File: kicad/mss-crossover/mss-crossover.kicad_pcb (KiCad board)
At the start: 2 copper layers, 76.2 x 57.2 mm, 64 parts, among them J1 Screw_Terminal_01x02, J10 SM04B-SRSS, J2 Screw_Terminal_01x02, J3 Screw_Terminal_01x02, J4 Screw_Terminal_01x02, J5 690-005-299-043, J6 SM04B-SRSS, J7 Micro_SD_Card_Det_Hirose_DM3AT, J8 Screw_Terminal_01x02, J9 Conn_01x05, SW1 FSM4JSMATR, SW2 FSM4JSMATR, U1 AP63203WU, U2 ESP32-S2-SOLO, U3 MAX98357AETE+T

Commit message: Initial PCB layout complete on v2.0
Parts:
- removed C10, C11, C12, C14, C15, C16, C17: 1uF, Capacitor_SMD:C_0805_2012Metric
- removed C13, C7, C9: 0.1uF, Capacitor_SMD:C_0805_2012Metric
- removed C8: 10uF, Capacitor_SMD:C_0805_2012Metric
- removed J10, J6: SM04B-SRSS, Connector_JST:JST_SH_SM04B-SRSS-TB_1x04-1MP_P1.00mm_Horizontal
- removed J5: 690-005-299-043, digikey-footprints:USB_Mini_B_Female_690-005-299-043
- removed J7: Micro_SD_Card_Det_Hirose_DM3AT, Connector_Card:microSD_HC_Hirose_DM3AT-SF-PEJM5
- removed J8: Screw_Terminal_01x02, TerminalBlock_MetzConnect:TerminalBlock_MetzConnect_Type059_RT06303HBWC_1x03_P3.50mm_Horizontal
- removed J9: Conn_01x05, Connector_PinHeader_2.54mm:PinHeader_1x05_P2.54mm_Vertical
- removed JP1, JP2: Conn_01x02, Connector_PinHeader_2.54mm:PinHeader_1x02_P2.54mm_Vertical
- removed L1: 4.7uH, ISE_UltraLibrarian:MSS6132-xxxMLC
- removed R10, R11, R12, R9: 1k, Resistor_SMD:R_0805_2012Metric
- removed R13, R14, R8: 10k, Resistor_SMD:R_0805_2012Metric
- removed R7: DNI, Resistor_SMD:R_0805_2012Metric
- removed SW2: FSM4JSMATR, digikey-footprints:Switch_Tactile_SMD_6x6mm
- removed TP1, TP2, TP3, TP4, TP5, TP6: TestPoint, TestPoint:TestPoint_Pad_D2.0mm
- added D6: GREEN LED, LED_SMD:LED_0805_2012Metric, F.Cu at (51.8, 187.6)
- added D7: RED LED, LED_SMD:LED_0805_2012Metric, F.Cu at (66.5, 187.6)
- added D8: AMBER LED, LED_SMD:LED_0805_2012Metric, F.Cu at (58.8, 187.6)
- added D9: SMAJ18A-TP, Diode_SMD:D_SMA, F.Cu at (71.4, 175.1)
- added F1: 1210L020WR, Resistor_SMD:R_1210_3225Metric, F.Cu at (69.7, 165.7)
- added T1: PE-51687, ISE_Generic:XFMR_PE-51687, F.Cu at (44.3, 159.2)
- added U4: TLP241A, ISE_UltraLibrarian:11-5B201S_TOS, F.Cu at (66.0, 175.1)
- C2: value 10uF -> 22uF
- C3: value 0.1uF -> 1uF
- C4, C5: value 22uF -> 0.1uF
- C6: value 10uF -> 0.1uF
- D1, D2: value D_Schottky -> CDBM140G
- D3: value GREEN LED -> CDBM140G; footprint LED_SMD:LED_0805_2012Metric -> Diode_SMD:D_SOD-123
- D4: value RED LED -> CDBM140G; footprint LED_SMD:LED_0805_2012Metric -> Diode_SMD:D_SOD-123
- D5: value RED LED -> BAV99; footprint LED_SMD:LED_0805_2012Metric -> Package_TO_SOT_SMD:SOT-23
- J2: value Screw_Terminal_01x02 -> AVR-ISP; footprint TerminalBlock_MetzConnect:TerminalBlock_MetzConnect_Type059_RT06303HBWC_1x03_P3.50mm_Horizontal -> Connector:Tag-Connect_TC2030-IDC-NL_2x03_P1.27mm_Vertical
- J3, J4: value Screw_Terminal_01x02 -> 8P8C; footprint TerminalBlock_MetzConnect:TerminalBlock_MetzConnect_Type059_RT06303HBWC_1x03_P3.50mm_Horizontal -> Connector_RJ:RJ45_Amphenol_54602-x08_Horizontal
- R3: value 330 -> 1k
- R4: value 330 -> 510
- R5: value 330 -> 100k
- R6: value DNI -> 330
- SW1: footprint digikey-footprints:Switch_Tactile_SMD_6x6mm -> ISE_Generic:TE_FSM4JSMA
- U1: value AP63203WU -> AP7381-33Y; footprint Package_TO_SOT_SMD:TSOT-23-6 -> ISE_Generic:SOT-89-3
- U2: value ESP32-S2-SOLO -> INA180A4; footprint Espressif:ESP32-S2-SOLO -> Package_TO_SOT_SMD:SOT-23-5
- U3: value MAX98357AETE+T -> ATtiny85-20S; footprint ISE_UltraLibrarian:21-0136I_T1633-4_MXM -> Package_SO:SOIC-8W_5.3x5.3mm_P1.27mm
- moved D4 59.2 mm to (30.6, 168.9), turned to -90 degrees
- moved D5 50.2 mm to (44.9, 167.1), turned to -90 degrees
- moved R6 47.0 mm to (64.9, 182.5)
- moved U3 36.8 mm to (55.5, 180.1)
- moved R4 36.0 mm to (48.5, 167.1)
- moved SW1 34.2 mm to (61.0, 161.0), turned to -90 degrees
- moved R5 27.5 mm to (59.0, 172.2), turned to 180 degrees
- moved C6 24.4 mm to (51.4, 167.1), turned to -90 degrees
- moved R1 23.8 mm to (51.8, 185.0), turned to 180 degrees
- moved U2 21.8 mm to (54.7, 171.1), turned to 180 degrees
- moved U1 19.9 mm to (42.8, 186.3), turned to -90 degrees
- moved D3 19.8 mm to (39.8, 168.9), turned to -90 degrees
- moved J4 19.6 mm to (86.7, 167.8), turned to 180 degrees
- moved H3 19.2 mm to (94.7, 158.0)
- moved H4 19.1 mm to (29.7, 158.0)
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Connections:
- C2 pad 1: /VPWR -> +3.3V
- C3 pad 1: Net-(C3-Pad1) -> /DCC_CURRENT
- C3 pad 2: Net-(C3-Pad2) -> GND
- C4 pad 1: +3.3V -> //CAL_SW
- C6 pad 1: +3.3V -> Net-(D5-Pad1)
- C6 pad 2: GND -> +3.3V
- D3 pad 1: GND -> Net-(D2-Pad2)
- D3 pad 2: Net-(D3-Pad2) -> GND
- D4 pad 1: GND -> Net-(D1-Pad2)
- D4 pad 2: Net-(D4-Pad2) -> GND
- D5 pad 1: GND -> Net-(D5-Pad1)
- D5 pad 2: Net-(D5-Pad2) -> Net-(D5-Pad1)
- J1 pad 1: Net-(D2-Pad2) -> Net-(D1-Pad2)
- J1 pad 2: GND -> Net-(D2-Pad2)
- J2 pad 1: /VPWR -> Net-(J2-Pad1)
- J2 pad 2: /VPWR -> +3.3V
- J2 pad 3: /VPWR -> Net-(J2-Pad3)
- J3 pad 1: GND -> Net-(J3-Pad1)
- J3 pad 2: GND -> Net-(J3-Pad2)
- J3 pad 3: GND -> Net-(J3-Pad3)
- J4 pad 1: Net-(J4-Pad1) -> Net-(J3-Pad3)
- J4 pad 2: GND -> Net-(J3-Pad6)
- J4 pad 3: Net-(J4-Pad3) -> Net-(J3-Pad1)
- R1 pad 1: Net-(J4-Pad1) -> Net-(D6-Pad2)
- R1 pad 2: /EN1 -> +3.3V
- R2 pad 1: Net-(J4-Pad3) -> Net-(J2-Pad1)
- R2 pad 2: /EN2 -> Net-(R2-Pad2)
- R3 pad 1: Net-(D3-Pad2) -> Net-(J2-Pad4)
- R3 pad 2: +3.3V -> Net-(R3-Pad2)
- R4 pad 1: Net-(D4-Pad2) -> +3.3V
- R4 pad 2: /LEDA -> Net-(D5-Pad1)
- R5 pad 1: Net-(D5-Pad2) -> /DCC_CURRENT
- R5 pad 2: /LEDB -> Net-(R5-Pad2)
- R6 pad 1: /GAIN_SLOT -> Net-(U4-Pad1)
- R6 pad 2: +3.3V -> Net-(J2-Pad1)
- SW1 pad 1: Net-(R11-Pad1) -> //CAL_SW
- SW1 pad 2: Net-(R11-Pad1) -> //CAL_SW
- U1 pad 2: /VPWR -> GND
- U2 pad 1: GND -> Net-(R5-Pad2)
- U2 pad 2: +3.3V -> GND
- U2 pad 3: /~{RST} -> Net-(D5-Pad1)
- U2 pad 4: /I2S_SD -> +3.3V
- U2 pad 5: /I2S_DATA -> +3.3V
- U3 pad 1: /I2S_DATA -> Net-(J2-Pad5)
- U3 pad 2: /GAIN_SLOT -> //CAL_SW
- U3 pad 3: GND -> /DCC_CURRENT
- U3 pad 4: /I2S_SD -> GND
- U3 pad 5: unconnected-(U3-Pad5) -> Net-(J2-Pad4)
- U3 pad 6: unconnected-(U3-Pad6) -> Net-(J2-Pad1)
- U3 pad 7: +3.3V -> Net-(J2-Pad3)
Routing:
- net /AUX1: track 83.6 -> 0.00 mm, vias 2 -> 0
- net /AUX2: track 81.8 -> 0.00 mm, vias 2 -> 0
- net Net-(J8-Pad3): track 81.6 -> 0.00 mm, vias 2 -> 0
- net Net-(J8-Pad1): track 79.4 -> 0.00 mm, vias 2 -> 0
- net +3.3V: track 100.5 -> 61.5 mm, vias 17 -> 0
- net /LEDB: track 35.1 -> 0.00 mm
- net /LEDA: track 33.5 -> 0.00 mm
- net Net-(J3-Pad3): track 0.00 -> 32.4 mm
- net /SDDET: track 32.1 -> 0.00 mm
- net /EN2: track 31.4 -> 0.00 mm
- net Net-(D3-Pad2): track 30.2 -> 0.00 mm
- net /EN1: track 29.8 -> 0.00 mm
- net /VOLDN: track 29.5 -> 0.00 mm
- net /MSS_OCC: track 0.00 -> 29.5 mm, vias 0 -> 3
- net /VOLUP: track 29.4 -> 0.00 mm
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- added copper zone on B.Cu, net /MSS_GND
- added copper zone on F.Cu, net //CAL_SW
- removed copper zone on B.Cu, net +3.3V
- removed copper zone on F.Cu, net +3.3V
- removed copper zone on F.Cu, net /MPJ6
- removed copper zone on F.Cu, net /VPWR
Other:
- board size 76.2 x 57.2 mm -> 73.7 x 38.1 mm
- board text added: "6-24 Volts DC/AC/DCC"
- board text added: "CAL"
- board text added: "DETECT"
- board text added: "Iowa Scaled Engineering MSS-CROSSOVER v2.0 www.iascaled.com (C)2024"
- board text added: "MSS"
- board text added: "POWER"
- board text removed: "*"
- board text removed: "A"
- board text removed: "B"
- board text removed: "GND"
- board text removed: "IN1 G IN2"
- board text removed: "IN3 G IN4"
- board text removed: "Iowa Scaled Engineering CKT-SOUNDPLAY v1.2 ©2023 CC BY-SA"
- board text removed: "SNS GND (BLK)"
- board text removed: "SNS PWR (RED)"
- board text removed: "SPK OUT"
- board text removed: "VIN"
- board text removed: "VOL DN"
- board text removed: "VOL UP"

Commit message: Updates per review
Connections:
- net //CAL_SW renamed /~{CAL_SW}
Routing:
- net GND: vias 25 -> 26
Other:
- board text added: "*"
- board text added: "Iowa Scaled Engineering MSS-CROSSOVER v2.0 www.iascaled.com ©2024"
- board text removed: "Iowa Scaled Engineering MSS-CROSSOVER v2.0 www.iascaled.com (C)2024"

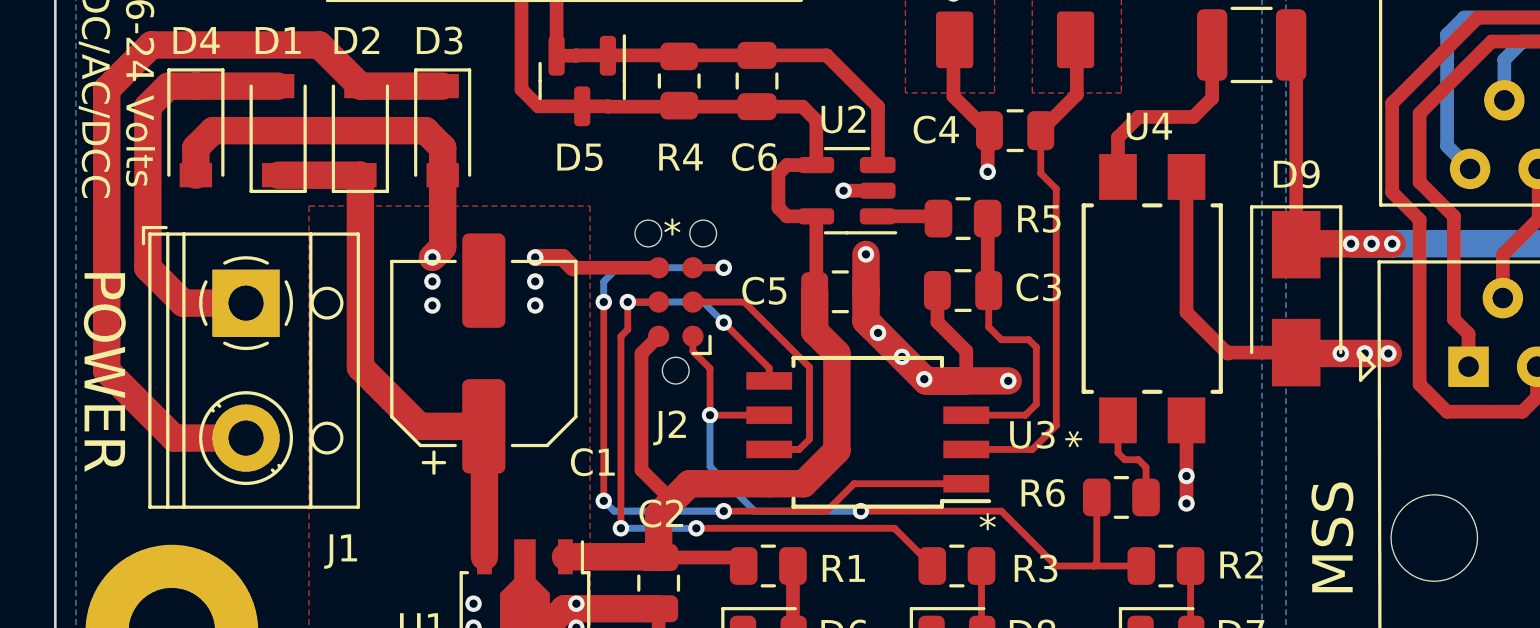
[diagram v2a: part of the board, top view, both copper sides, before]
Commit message: Add test points
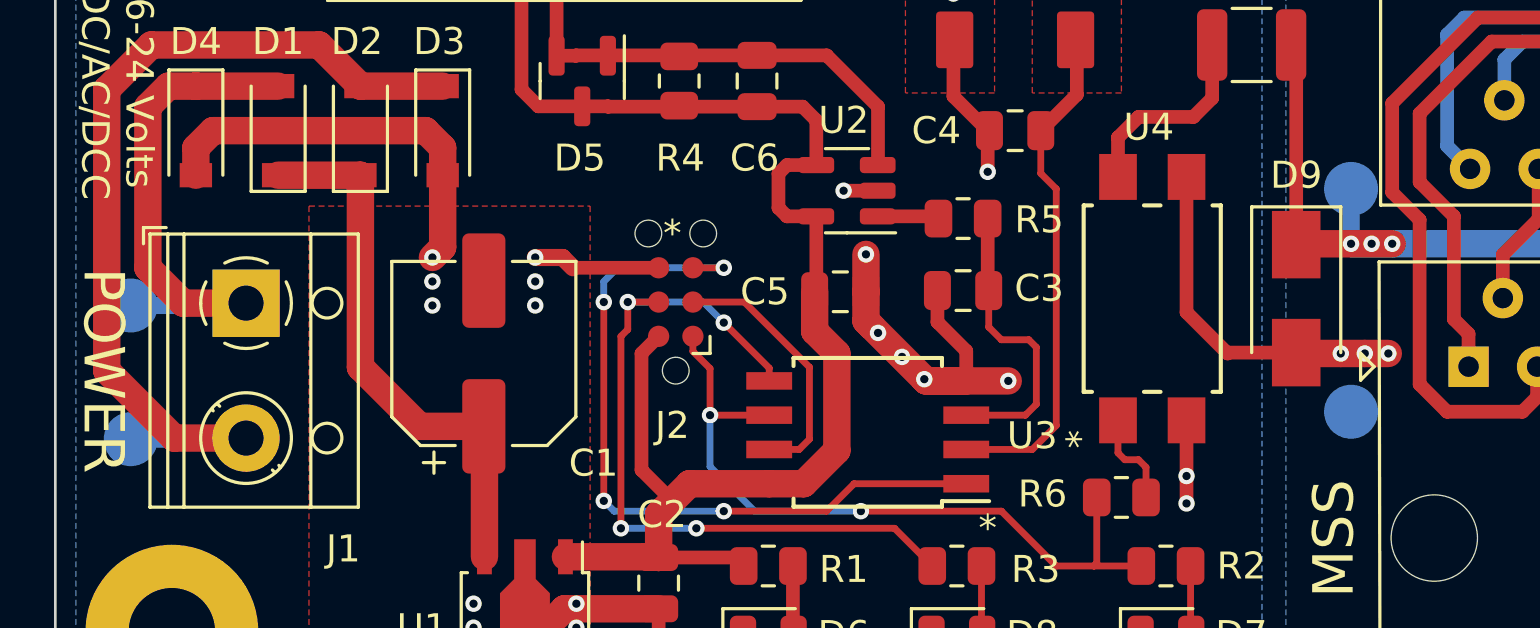
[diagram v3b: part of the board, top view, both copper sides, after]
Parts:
- added TP1: TestPoint, TestPoint:TestPoint_Pad_D2.0mm, B.Cu at (28.2, 175.4)
- added TP2: TestPoint, TestPoint:TestPoint_Pad_D2.0mm, B.Cu at (28.2, 180.3)
- added TP3: TestPoint, TestPoint:TestPoint_Pad_D2.0mm, B.Cu at (73.4, 171.1)
- added TP4: TestPoint, TestPoint:TestPoint_Pad_D2.0mm, B.Cu at (73.4, 179.3)
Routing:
- net Net-(D1-Pad2): track 15.3 -> 19.6 mm
- net Net-(D2-Pad2): track 30.4 -> 34.7 mm
- net /MSS_OCC: track 29.5 -> 31.5 mm
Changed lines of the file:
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@@
       (net 2 "GND") (pintype "passive") (solder_mask_margin 0.102) (zone_connect 2))
+  )
+  (footprint "TestPoint:TestPoint_Pad_D2.0mm" (layer "B.Cu")
+    (at 73.406 179.324 180)
+    (descr "SMD pad as test Point, diameter 2.0mm")
+    (tags "test point SMD pad")
+    (property "Sheetfile" "mss-crossover.kicad_sch")
+    (property "Sheetname" "")
+    (zone_connect 2)
+    (attr exclude_from_pos_files)
+    (fp_text reference "TP4" (at 0 1.998) (layer "B.SilkS")
+      (effects (font (size 1 1) (thickness 0.15)) (justify mirror))
+    )
+    (fp_text value "TestPoint" (at 0 -2.05) (layer "B.Fab")
+      (effects (font (size 1 1) (thickness 0.15)) (justify mirror))
+    )
+    (fp_text user "${REFERENCE}" (at 0 2) (layer "B.Fab")
+      (effects (font (size 1 1) (thickness 0.15)) (justify mirror))
+    )
+    (fp_circle (center 0 0) (end 0 -1.2) (layer "B.SilkS") (width 0.12) (fill none))
+    (fp_circle (center 0 0) (end 1.5 0) (layer "B.CrtYd") (width 0.05) (fill none))
+    (pad "1" smd circle (at 0 0 180) (size 2 2) (layers "B.Cu" "B.Mask")
+      (net 14 "/MSS_GND") (pinfunction "1") (pintype "passive"))
+  )
+  (footprint "TestPoint:TestPoint_Pad_D2.0mm" (layer "B.Cu")
+    (at 73.406 171.069 180)
+    (descr "SMD pad as test Point, diameter 2.0mm")
+    (tags "test point SMD pad")
+    (property "Sheetfile" "mss-crossover.kicad_sch")
+    (property "Sheetname" "")
+    (attr exclude_from_pos_files)
+    (fp_text reference "TP3" (at 0 1.998) (layer "B.SilkS")
+      (effects (font (size 1 1) (thickness 0.15)) (justify mirror))
+    )
+    (fp_text value "TestPoint" (at 0 -2.05) (layer "B.Fab")
+      (effects (font (size 1 1) (thickness 0.15)) (justify mirror))
+    )
+    (fp_text user "${REFERENCE}" (at 0 2) (layer "B.Fab")
+      (effects (font (size 1 1) (thickness 0.15)) (justify mirror))
+    )
+    (fp_circle (center 0 0) (end 0 -1.2) (layer "B.SilkS") (width 0.12) (fill none))
+    (fp_circle (center 0 0) (end 1.5 0) (layer "B.CrtYd") (width 0.05) (fill none))
+    (pad "1" smd circle (at 0 0 180) (size 2 2) (layers "B.Cu" "B.Mask")
+      (net 13 "/MSS_OCC") (pinfunction "1") (pintype "passive"))
+  )
+  (footprint "TestPoint:TestPoint_Pad_D2.0mm" (layer "B.Cu")
+    (at 28.194 180.34 180)
+    (descr "SMD pad as test Point, diameter 2.0mm")
+    (tags "test point SMD pad")
+    (property "Sheetfile" "mss-crossover.kicad_sch")
+    (property "Sheetname" "")
+    (attr exclude_from_pos_files)
+    (fp_text reference "TP2" (at 0 1.998) (layer "B.SilkS")
+      (effects (font (size 1 1) (thickness 0.15)) (justify mirror))
+    )
+    (fp_text value "TestPoint" (at 0 -2.05) (layer "B.Fab")
+      (effects (font (size 1 1) (thickness 0.15)) (justify mirror))
+    )
+    (fp_text user "${REFERENCE}" (at 0 2) (layer "B.Fab")
+      (effects (font (size 1 1) (thickness 0.15)) (justify mirror))
+    )
+    (fp_circle (center 0 0) (end 0 -1.2) (layer "B.SilkS") (width 0.12) (fill none))
+    (fp_circle (center 0 0) (end 1.5 0) (layer "B.CrtYd") (width 0.05) (fill none))
+    (pad "1" smd circle (at 0 0 180) (size 2 2) (layers "B.Cu" "B.Mask")
+      (net 6 "Net-(D2-Pad2)") (pinfunction "1") (pintype "passive"))
+  )
+  (footprint "TestPoint:TestPoint_Pad_D2.0mm" (layer "B.Cu")
+    (at 28.194 175.387 180)
+    (descr "SMD pad as test Point, diameter 2.0mm")
+    (tags "test point SMD pad")
+    (property "Sheetfile" "mss-crossover.kicad_sch")
+    (property "Sheetname" "")
+    (attr exclude_from_pos_files)
+    (fp_text reference "TP1" (at 0 1.998) (layer "B.SilkS")
+      (effects (font (size 1 1) (thickness 0.15)) (justify mirror))
+    )
+    (fp_text value "TestPoint" (at 0 -2.05) (layer "B.Fab")
+      (effects (font (size 1 1) (thickness 0.15)) (justify mirror))
+    )
+    (fp_text user "${REFERENCE}" (at 0 2) (layer "B.Fab")
+      (effects (font (size 1 1) (thickness 0.15)) (justify mirror))
+    )
+    (fp_circle (center 0 0) (end 0 -1.2) (layer "B.SilkS") (width 0.12) (fill none))
+    (fp_circle (center 0 0) (end 1.5 0) (layer "B.CrtYd") (width 0.05) (fill none))
+    (pad "1" smd circle (at 0 0 180) (size 2 2) (layers "B.Cu" "B.Mask")
+      (net 5 "Net-(D1-Pad2)") (pinfunction "1") (pintype "passive"))
   )
   (gr_poly
@@
   (segment (start 28.829 173.99) (end 30.139 175.3) (width 1.016) (layer "F.Cu") (net 5))
   (segment (start 30.607 167.26) (end 29.59 167.26) (width 1.016) (layer "F.Cu") (net 5))
+  (segment (start 28.194 175.387) (end 32.379 175.387) (width 0.635) (layer "B.Cu") (net 5))
+  (segment (start 32.379 175.387) (end 32.466 175.3) (width 0.635) (layer "B.Cu") (net 5))
   (segment (start 28.956 165.735) (end 35.178 165.735) (width 1.016) (layer "F.Cu") (net 6))
   (segment (start 27.305 167.386) (end 28.956 165.735) (width 1.016) (layer "F.Cu") (net 6))
@@
   (segment (start 36.703 167.26) (end 39.751 167.26) (width 1.016) (layer "F.Cu") (net 6))
   (segment (start 27.305 177.8) (end 27.305 167.386) (width 1.016) (layer "F.Cu") (net 6))
+  (segment (start 32.426 180.34) (end 32.466 180.3) (width 0.635) (layer "B.Cu") (net 6))
+  (segment (start 28.194 180.34) (end 32.426 180.34) (width 0.635) (layer "B.Cu") (net 6))
   (segment (start 63.246 167.574) (end 63.246 165.591) (width 0.508) (layer "F.Cu") (net 7))
   (segment (start 59.149 180.721) (end 61.595 180.721) (width 0.254) (layer "F.Cu") (net 7))
@@
   (segment (start 82.931 170.307) (end 82.931 170.942) (width 1.016) (layer "B.Cu") (net 13))
   (segment (start 81.5695 175.113) (end 81.5695 173.8985) (width 1.016) (layer "B.Cu") (net 13))
+  (segment (start 73.406 173.101) (end 73.406 171.069) (width 0.635) (layer "B.Cu") (net 13))
   (segment (start 74.168 173.101) (end 73.406 173.101) (width 1.016) (layer "B.Cu") (net 13))
   (segment (start 81.5695 173.8985) (end 80.772 173.101) (width 1.016) (layer "B.Cu") (net 13))
